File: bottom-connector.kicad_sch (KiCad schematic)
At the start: 10 parts, among them J1 ELP-000097, J2 ELP-000029, J3 ELP-000063, U1 ELP-000052

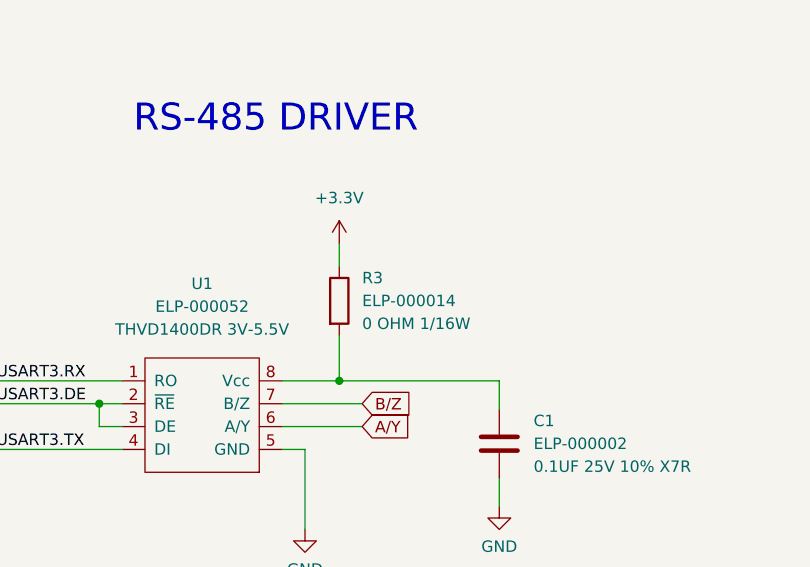
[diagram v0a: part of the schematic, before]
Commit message: Fixed errors on the schematic found after fabrication of the X1 PCB's.
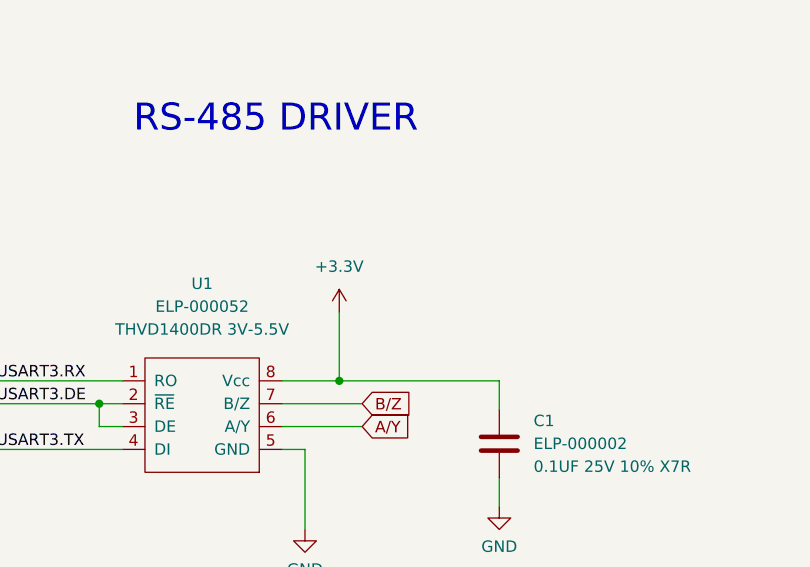
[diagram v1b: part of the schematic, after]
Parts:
- removed R3: ELP-000014, 1_EarthLCD:R_0402_1005Metric, symbol 1_EarthLCD:ELP-000014
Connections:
- net +3.3V: now also C1.1, U1.8 (Vcc)
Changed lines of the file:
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@@
     (stroke (width 0) (type default))
   )
-  (wire (pts (xy 83.82 127) (xy 83.82 129.54))
+  (wire (pts (xy 83.82 134.62) (xy 83.82 142.24))
     (stroke (width 0) (type default))
   )
@@
   )
   (wire (pts (xy 69.85 34.29) (xy 90.17 34.29))
-    (stroke (width 0) (type default))
-  )
-  (wire (pts (xy 83.82 137.16) (xy 83.82 142.24))
     (stroke (width 0) (type default))
   )
@@
     )
   )
-  (symbol (lib_id "power:+3.3V") (at 83.82 127 0) (unit 1)
-    (in_bom yes) (on_board yes) (dnp no) (fields_autoplaced)
-    (property "Reference" "#PWR04" (at 83.82 130.81 0)
-      (effects (font (size 1.27 1.27)) hide)
-    )
-    (property "Value" "+3.3V" (at 83.82 121.92 0)
-      (effects (font (size 1.27 1.27)))
-    )
-    (property "Footprint" "" (at 83.82 127 0)
-      (effects (font (size 1.27 1.27)) hide)
-    )
-    (property "Datasheet" "" (at 83.82 127 0)
+  (symbol (lib_id "power:+3.3V") (at 83.82 134.62 0) (unit 1)
+    (in_bom yes) (on_board yes) (dnp no) (fields_autoplaced)
+    (property "Reference" "#PWR04" (at 83.82 138.43 0)
+      (effects (font (size 1.27 1.27)) hide)
+    )
+    (property "Value" "+3.3V" (at 83.82 129.54 0)
+      (effects (font (size 1.27 1.27)))
+    )
+    (property "Footprint" "" (at 83.82 134.62 0)
+      (effects (font (size 1.27 1.27)) hide)
+    )
+    (property "Datasheet" "" (at 83.82 134.62 0)
       (effects (font (size 1.27 1.27)) hide)
     )
@@
         )
       )
-    )
-  )
-  (symbol (lib_id "1_EarthLCD:ELP-000014") (at 83.82 133.35 0) (unit 1)
-    (in_bom yes) (on_board yes) (dnp no) (fields_autoplaced)
-    (property "Reference" "R3" (at 86.36 130.8099 0)
-      (effects (font (size 1.27 1.27)) (justify left))
-    )
-    (property "Value" "ELP-000014" (at 86.36 133.3499 0)
-      (effects (font (size 1.27 1.27)) (justify left))
-    )
-    (property "Footprint" "1_EarthLCD:R_0402_1005Metric" (at 82.042 133.35 90)
-      (effects (font (size 1.27 1.27)) hide)
-    )
-    (property "Datasheet" "~" (at 83.82 133.35 0)
-      (effects (font (size 1.27 1.27)) hide)
-    )
-    (property "Info" "0 OHM 1/16W" (at 86.36 135.8899 0)
-      (effects (font (size 1.27 1.27)) (justify left))
-    )
-    (property "Earth" "RES-0-1/6W-0402" (at 88.9 133.35 90)
-      (effects (font (size 1.27 1.27)) hide)
-    )
-    (pin "1")
-    (pin "2")
-    (instances
-      (project "ezLCD-303-PicoPi-Breakout-Board"
-        (path "/00955ca7-e382-491b-9e67-f8c537447774/107ae0b7-6f32-49a5-aebd-43a6142a295e"
-          (reference "R3") (unit 1)
-        )
-      )
-      (project "PCB-2301"
-        (path "/1ded335d-6d13-4ffa-94d5-e15dc2cb695c/d4a07de9-06a8-4cb3-8ea5-718fa4e90a32"
-          (reference "R42") (unit 1)
-        )
-      )
